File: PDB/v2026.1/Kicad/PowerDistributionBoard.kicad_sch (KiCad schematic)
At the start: 78 parts, among them J1 12V_EXP3, J10 BMS, J11 IMD, J12 Suspension_Linear_Pot1, J13 Suspension_Linear_Pot2, J14 Suspension_Linear_Pot3, J15 Suspension_Linear_Pot4, J16 CCM_Faults, J17 EXP1_5V, J18 RasPI_5V, J19 LATCH_12V, J2 12V_EXP2, J20 Throttle_Sensor, J21 Current_Sensor, J22 Brake_Sensor1, J23 Brake_Sensor2, J24 Wheel_Sensor1, J25 Wheel_Sensor2, J26 3V3_EXP, J27 BATTERY_12V, J28 BATTERY_GND, J29 BATTERY_24V, J3 12V_EXP1, J31 FAN1_24V, J32 FAN2_24V, J33 PUMP1_24V, J34 PUMP2_24V, J35 24V_EXP1, J4 RTM, J5 CCM_12V, J7 BSPD, J8 LATCH, J9 TSSI, U1 5to3.3_Linear_Regulator, U2 TLV76150DCYR

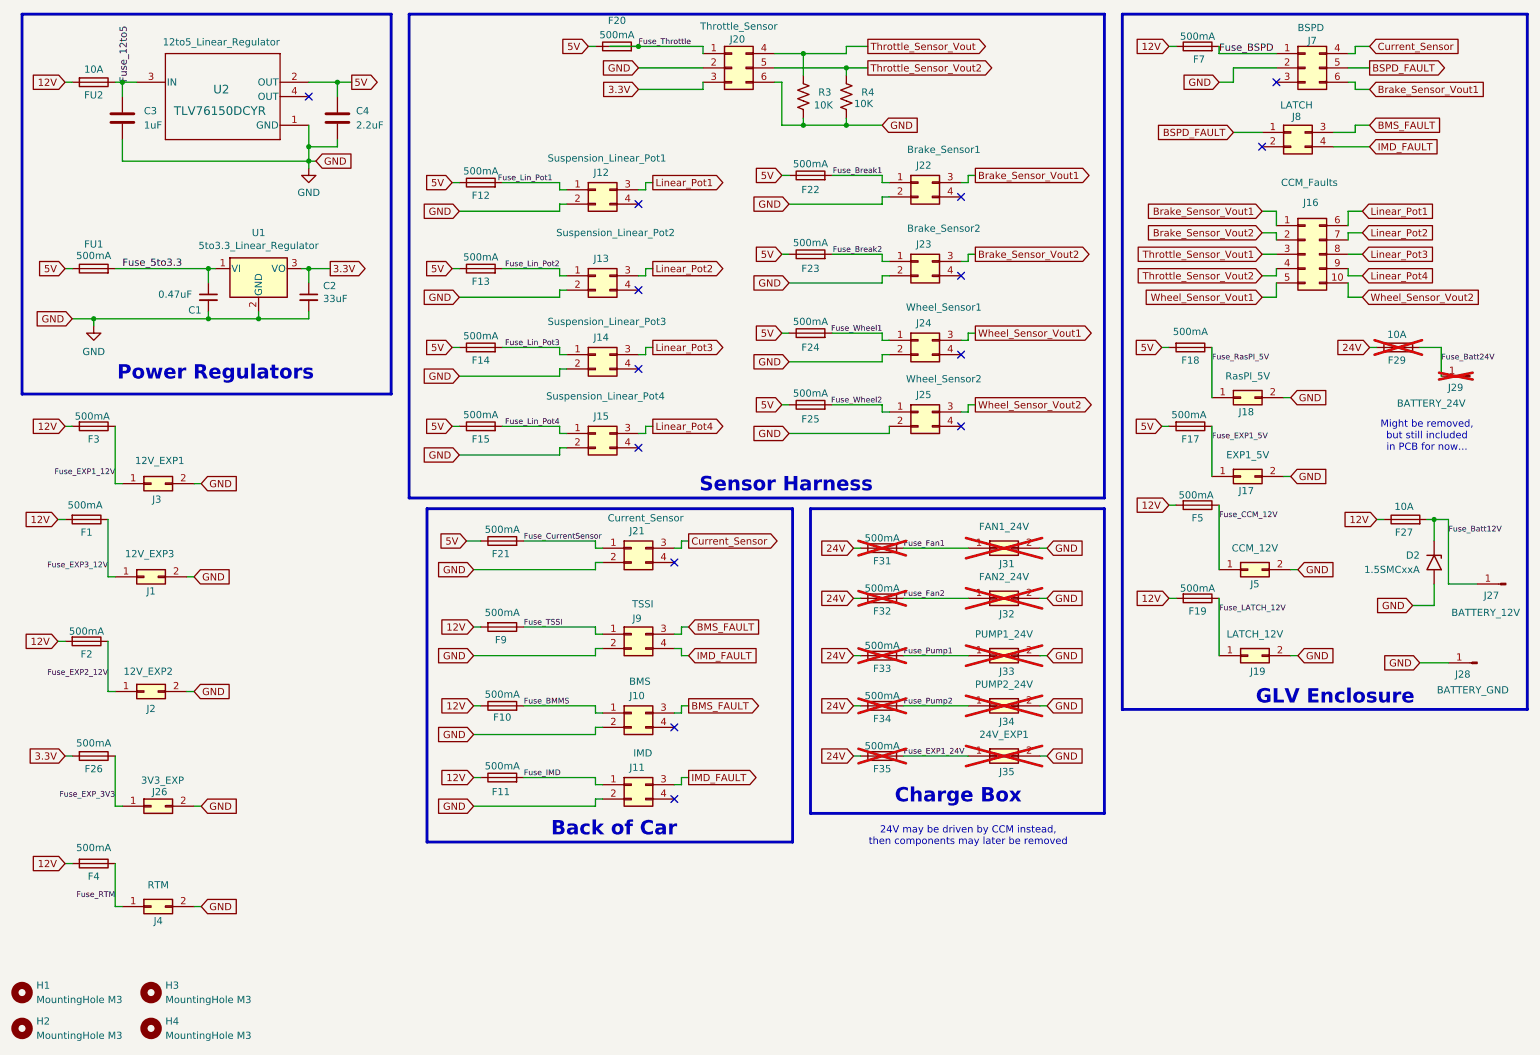
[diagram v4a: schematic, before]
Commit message: Started labeling each pin
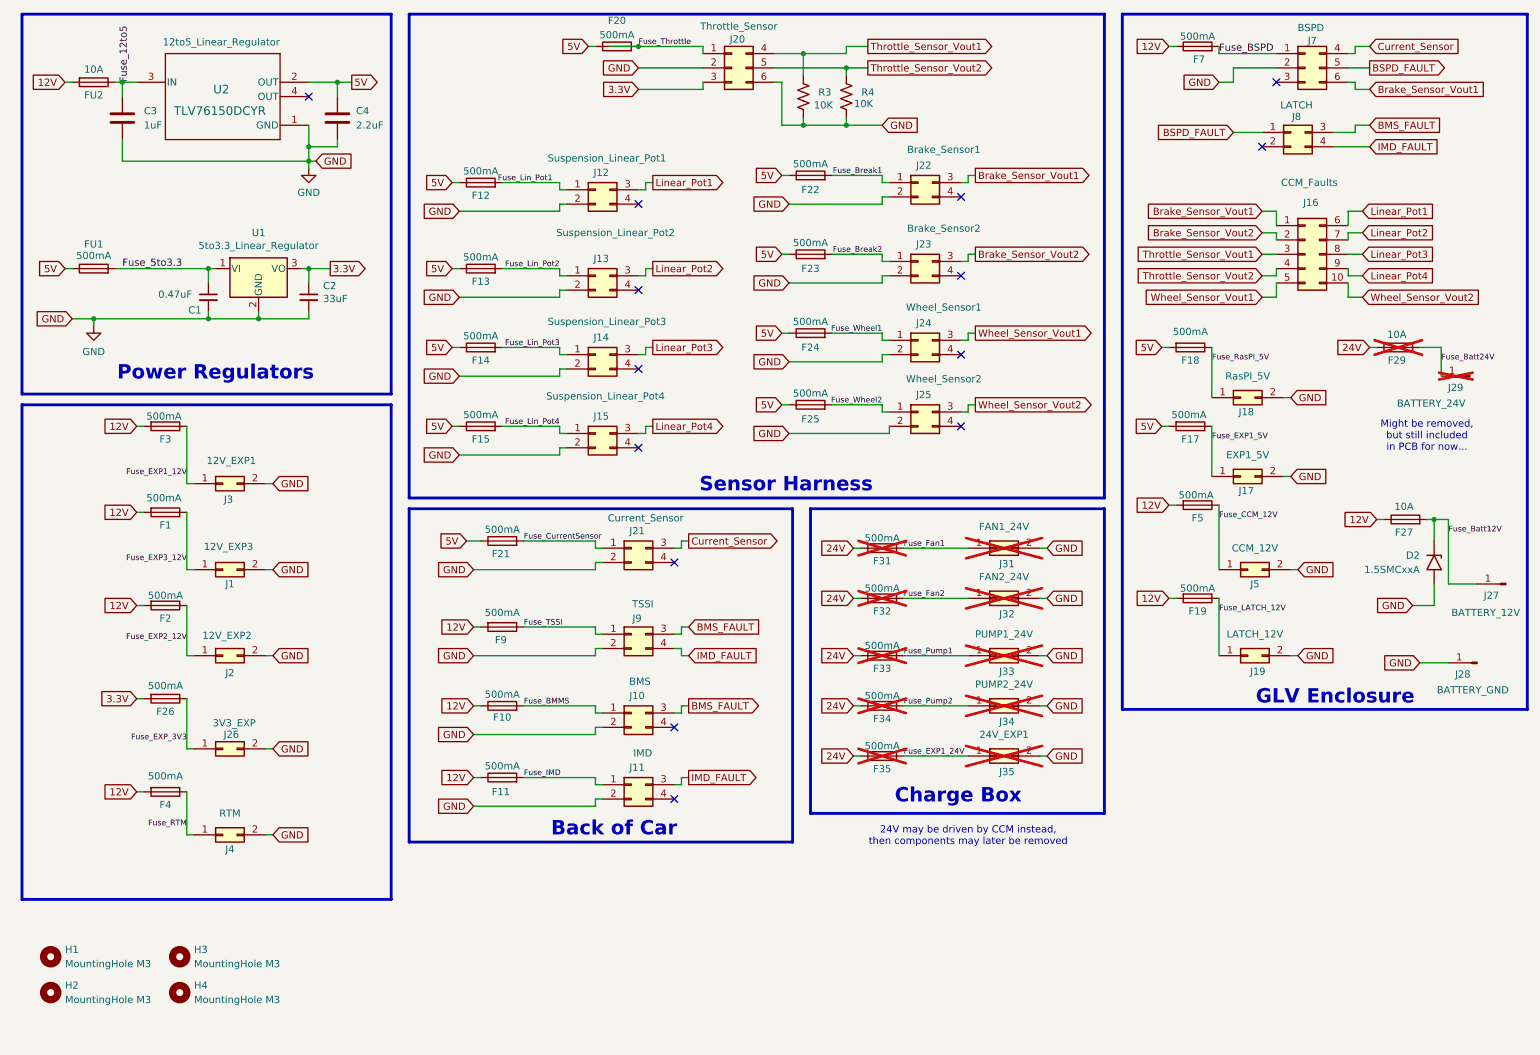
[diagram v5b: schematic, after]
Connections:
- net Throttle_Sensor_Vout is gone; now on net Throttle_Sensor_Vout1: J20.4 (Pin_4), R3.1
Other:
- moved on the sheet: F1, F2, F26, F3, F4, H1, H2, H3, H4, J1, J2, J26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

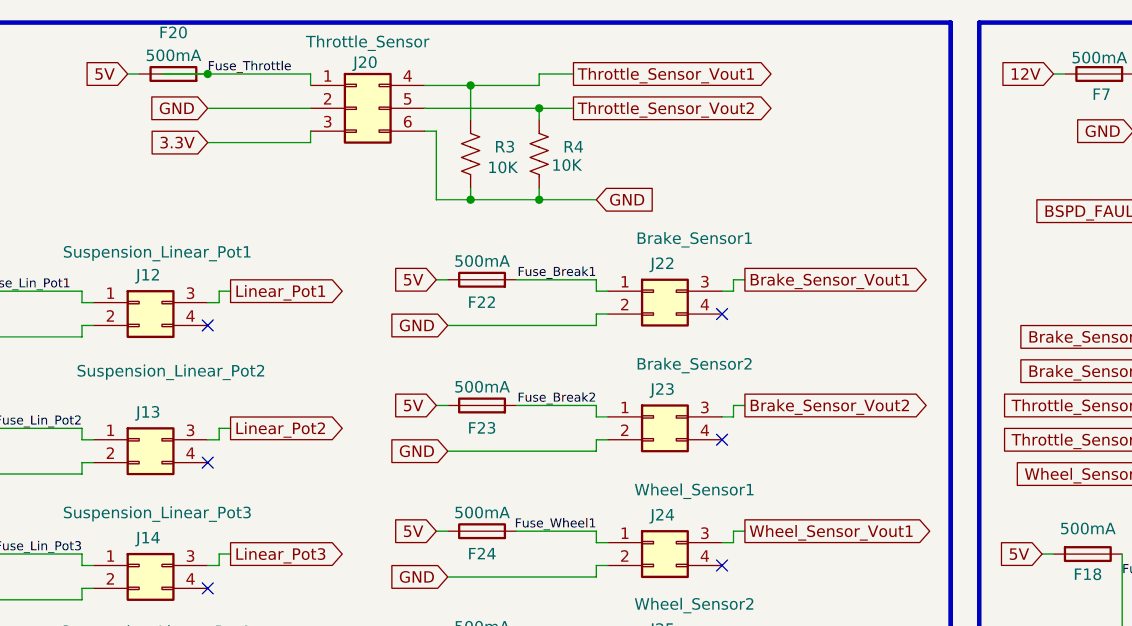
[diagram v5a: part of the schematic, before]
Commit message: Combined break pressure into Throttle sensor
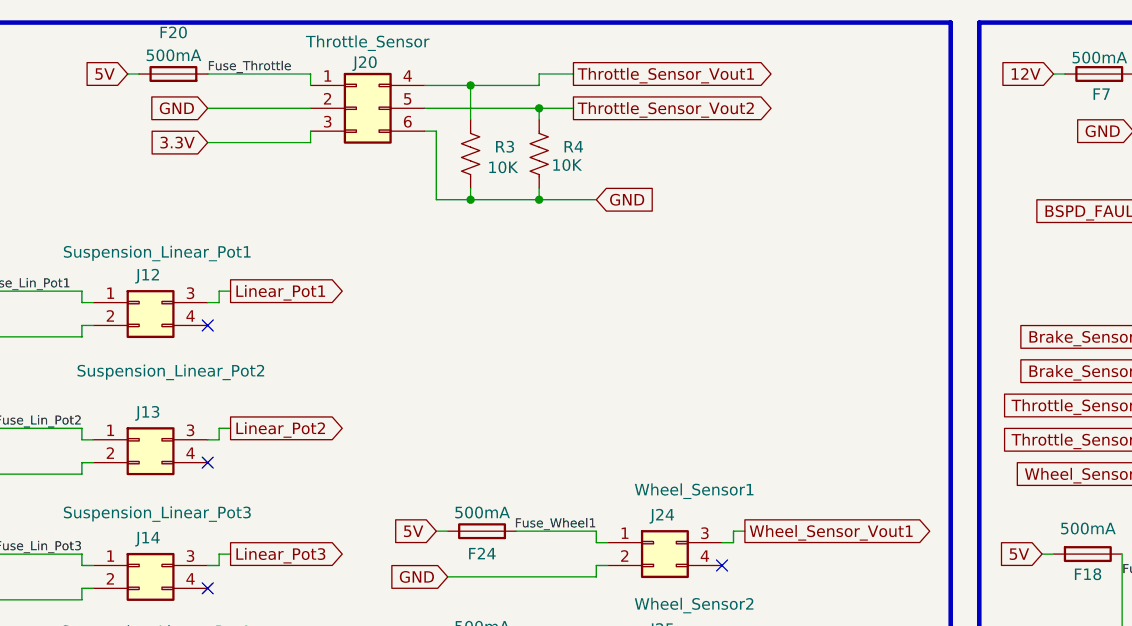
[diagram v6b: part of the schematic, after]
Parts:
- removed F22, F23: 500mA, 0footprints:649-SERIES-HOLDER, symbol Device:Fuse
- removed J22: Brake_Sensor1, 0footprints:Molex_Mini-Fit_Jr_5566-04A_2x02_P4.20mm_Vertical, symbol Connector_Generic:Conn_02x02_Top_Bottom
- removed J23: Brake_Sensor2, 0footprints:Molex_Mini-Fit_Jr_5566-04A_2x02_P4.20mm_Vertical, symbol Connector_Generic:Conn_02x02_Top_Bottom
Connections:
- no-connect marks 14 -> 12

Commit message: Added labels of possibly removeing 3V3 line
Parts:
- C1, C2, F26, FU1, J26, U1: now not fitted
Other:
- note added: "3V3 line may be removed"
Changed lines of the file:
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@@
 		)
 	)
+	(text "3V3 line \nmay be removed"
+		(exclude_from_sim no)
+		(at 70.866 150.368 0)
+		(effects
+			(font
+				(size 1.27 1.27)
+			)
+		)
+	)
+	(text "3V3 line \nmay be removed"
+		(exclude_from_sim no)
+		(at 70.612 71.374 0)
+		(effects
+			(font
+				(size 1.27 1.27)
+			)
+		)
+	)
 	(text "GLV Enclosure"
 		(exclude_from_sim no)
@@
 		(in_bom yes)
 		(on_board yes)
-		(dnp no)
+		(dnp yes)
 		(property "Reference" "U1"
 			(at 57.15 53.34 0)
@@
 		(in_bom yes)
 		(on_board yes)
-		(dnp no)
+		(dnp yes)
 		(property "Reference" "F26"
 			(at 40.64 138.176 90)
@@
 		(in_bom yes)
 		(on_board yes)
-		(dnp no)
+		(dnp yes)
 		(property "Reference" "C1"
 			(at 44.704 67.056 0)
@@
 		(in_bom yes)
 		(on_board yes)
-		(dnp no)
+		(dnp yes)
 		(property "Reference" "#PWR03"
 			(at 27.94 76.2 0)
@@
 		(in_bom yes)
 		(on_board yes)
-		(dnp no)
+		(dnp yes)
 		(property "Reference" "C2"
 			(at 68.58 62.738 0)
@@
 		(in_bom yes)
 		(on_board yes)
-		(dnp no)
+		(dnp yes)
 		(property "Reference" "J26"
 			(at 52.324 142.24 0)
@@
 		(in_bom yes)
 		(on_board yes)
-		(dnp no)
+		(dnp yes)
 		(property "Reference" "FU1"
 			(at 27.94 55.372 90)

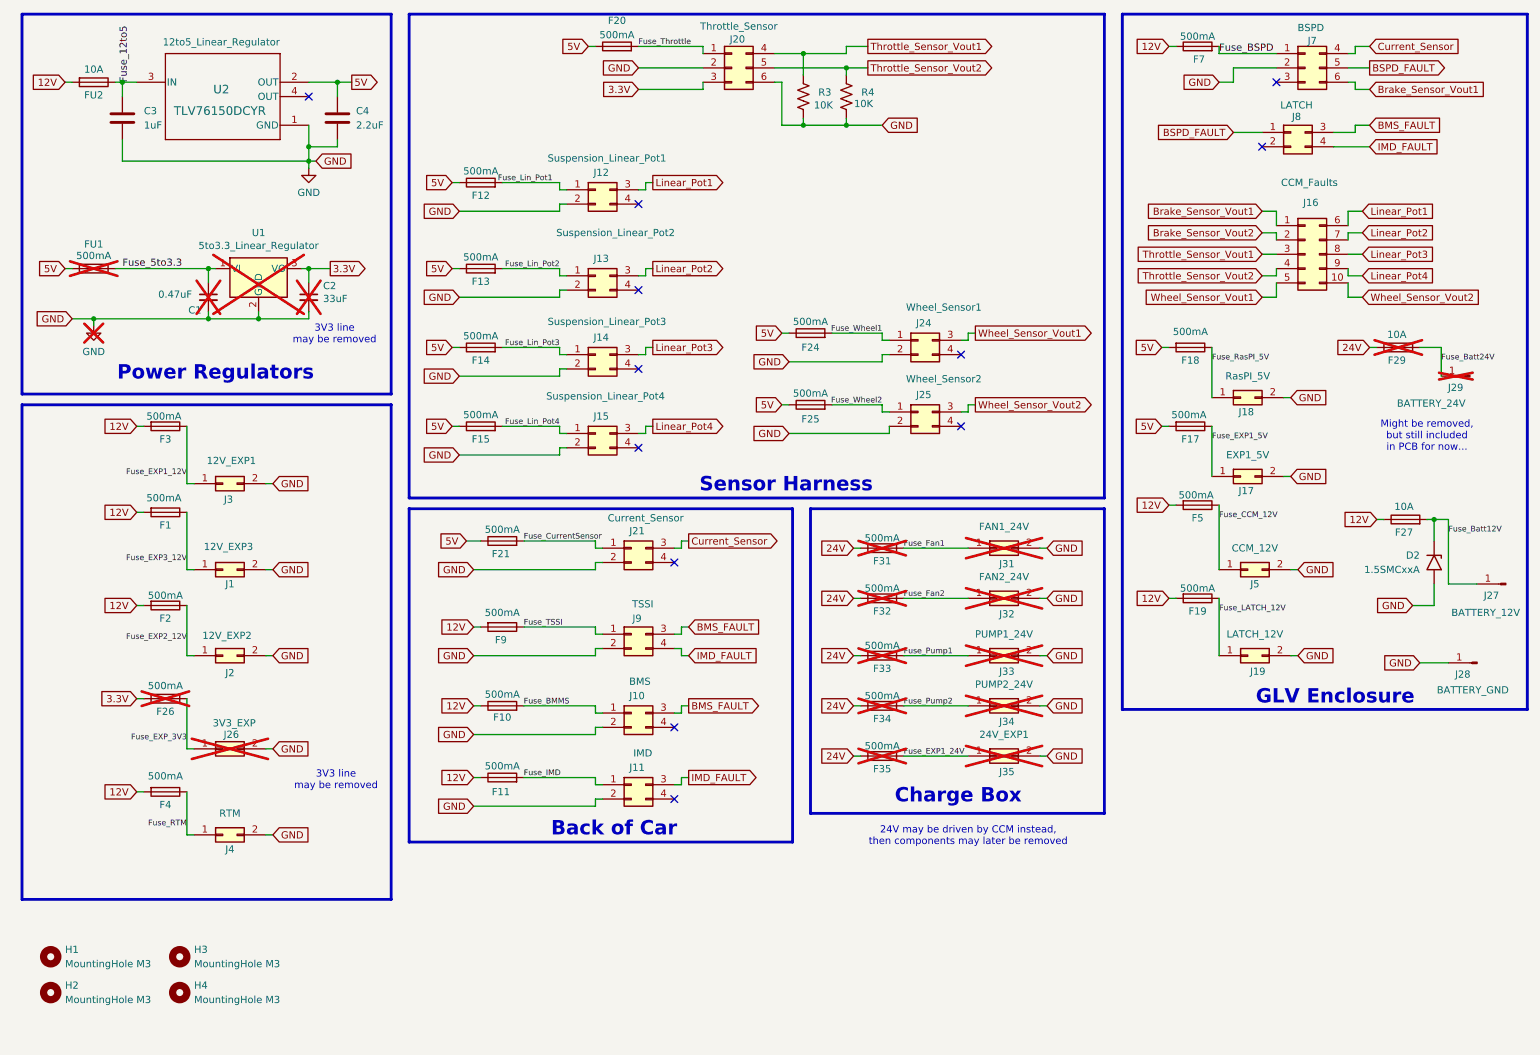
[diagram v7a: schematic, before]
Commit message: Added 24V line back
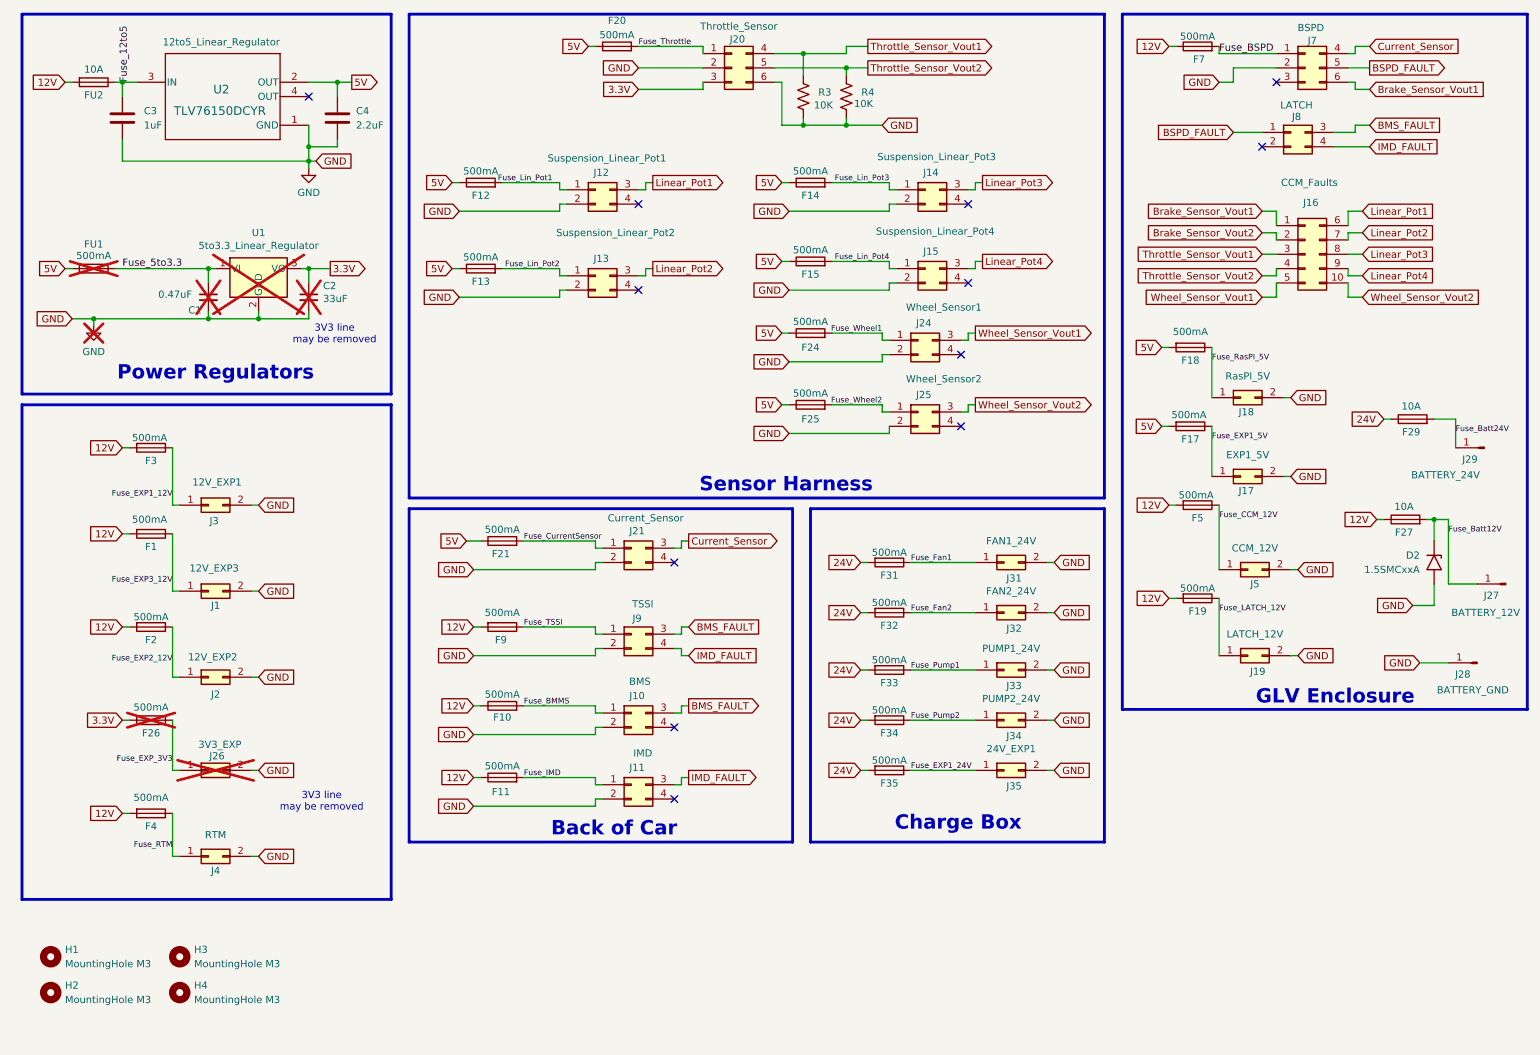
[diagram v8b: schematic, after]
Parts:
- F29, F31, F32, F33, F34, F35, J29, J31, J32, J33, J34, J35: now fitted
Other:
- note removed: "24V may be driven by CCM instead, then components may later be removed"
- note removed: "Might be removed, but still included in PCB for now..."
- moved on the sheet: F1, F14, F15, F2, F26, F3, F4, J1, J14, J15, J2, J26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
